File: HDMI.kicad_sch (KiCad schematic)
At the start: 38 parts, among them J1004 HDMI_D_1.4, Q1 2N7002, Q2 2SK3018, Q3 2SK3018, Q4 2SK3018, U1011 TPAZ1023-04F, U1012 TPAZ1023-04F

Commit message: commit before removing duplicated glasgow
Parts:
- renumbered C17 to C187, C1070 to C188, C1071 to C189, C1072 to C190, C1073 to C191, C1074 to C192, C1075 to C193, C1076 to C194, C1092 to C199, D1014 to D37, D1015 to D38, D1016 to D39, D1017 to D40, F1002 to F6, J1004 to J32, Q1 to Q11, Q2 to Q12, Q3 to Q13, Q4 to Q14, R1043 to R120, R1044 to R121, R1045 to R122, R1046 to R124, R1047 to R125, R1048 to R126, R1049 to R127, R1050 to R128, R1051 to R129, R1052 to R130, R1053 to R131, R1054 to R132, R1055 to R133, R1056 to R134, R1057 to R135, R1058 to R136, R1059 to R137, U1011 to U43, U1012 to U44

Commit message: went back to the drawing board
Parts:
- added C11, C14, C16, C18, C20, C22, C24, C26, C28, C30, C32, C34, C36, C38: 0.1uF, A_DFRobot:C_0402, symbol Device:C
- added C13, C15, C17, C19, C21, C23, C25, C27, C29, C31, C33, C35, C37, C39: 10nF, A_DFRobot:C_0402, symbol Device:C
- added C61, C62: 47pF, A_DFRobot:C_0402, symbol Device:C
- added C63, C64: 1uF, A_DFRobot:C_0402, symbol Device:C
- added D1, D27: RCLAMP0524PATCT, RCLAMP0524PATCT:DIO_RCLAMP0524PATCT, symbol RCLAMP0524PATCT:RCLAMP0524PATCT
- added D2: RCLAMP0524PATCT, HDMI:DIO_RCLAMP0524PATCT, symbol RCLAMP0524PATCT:RCLAMP0524PATCT
- added D28: LED, LED_SMD:LED_0603_1608Metric, symbol Device:LED
- added J3: Conn_01x03_Pin, symbol Connector:Conn_01x03_Pin
- added J4: Conn_02x01, symbol Connector_Generic:Conn_02x01
- added R10, R11, R12, R13, R14, R15, R17, R5, R6, R7, R8, R9: 0 Ohm, A_DFRobot:R_0603_1608Metric, symbol Device:R
- added R25, R26: 2k, A_DFRobot:R_0402, symbol Device:R
- added R28: 887ohm +-1%, A_DFRobot:R_0402, symbol Device:R
- added R29: 500ohm +-1%, A_DFRobot:R_0402, symbol Device:R
- added R86: 47k +-1%, A_DFRobot:R_0402, symbol Device:R
- added R87: 390k, A_DFRobot:R_0402, symbol Device:R
- added R88, R89: 51r, A_DFRobot:R_0402, symbol Device:R
- added R90: 5r1, A_DFRobot:R_0402, symbol Device:R
- added R91: 48k7, A_DFRobot:R_0402, symbol Device:R
- added R92: 220r, A_DFRobot:R_0402, symbol Device:R
- added TP2: ALSB, A_HDJ_Library:TestPoint_Pad_D1.0mm, symbol Connector:TestPoint
- added U1: ADV7623BSTZ, ST_144_ADI, symbol 2026-04-04_08-32-55:ADV7623BSTZ
- added U2: NC7SZ125M5, SC-74A-5_1P65X3P15_ONS, symbol 2026-04-05_20-11-58:NC7SZ125M5
- added Y3: ABM8G-28.63636MHZ-18-D2Y-T, CRYSTAL_ABM8G_ABR, symbol 2026-04-05_02-23-25:ABM8G-28.63636MHZ-18-D2Y-T
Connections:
- net +3V3: now also C24.1, C25.1, C26.1, C27.1, C28.1, C29.1, C30.1, C31.1, C32.1, C33.1, U1.114 (TVDD), U1.12 (TVDD), U1.120 (TVDD), U1.133 (TVDD), U1.139 (TVDD), U1.25 (TVDD), U1.31 (TVDD), U1.6 (TVDD), U1.73 (DVDDIO), U1.86 (DVDDIO), U2.5 (VCC)
- net 5V_HDMI_VCC: now also R25.1, R26.1
- net DDC_SCL: now also R14.1, U1.109 (DDCA_SCL); no longer J32.17 (SCL)
- net DDC_SDA: now also R15.1, U1.108 (DDCA_SDA); no longer J32.18 (SDA)
- net GND: now also C11.2, C13.2, C14.2, C15.2, C16.2, C17.2, C18.2, C19.2, C20.2, C21.2, C22.2, C23.2, C24.2, C25.2, C26.2, C27.2, C28.2, C29.2, C30.2, C31.2, C32.2, C33.2, C34.2, C35.2, C36.2, C37.2, C38.2, C39.2, C61.2, C62.2, D1.3_8, D2.3_8, D27.3_8, D28.1 (K), R28.2, R29.1, R90.2, R91.2, U1.104 (PGND), U1.111 (CGND), U1.117 (CGND), U1.125 (DGND), U1.130 (CGND), U1.136 (CGND), U1.17 (DGND), U1.22 (CGND), U1.28 (CGND), U1.3 (CGND), U1.35 (CGND), U1.38 (TXGND), U1.39 (TXPGND), U1.46 (TXGND), U1.49 (TXGND), U1.52 (TXGND), U1.58 (TXGND), U1.60 (DGND), U1.72 (DGNDIO), U1.80 (DGND), U1.85 (DGNDIO), U1.9 (CGND), U1.92 (DGND), U1.99 (PGND), U2.1 (*OE), U2.3 (GND), Y3.2 (GND), Y3.4 (GND)
- net HPD: now also R17.1, U1.105 (HP_CTRLA); no longer J32.1 (HPD/HEAC-)
- net TMDS_CK+: now also R11.1, U1.113 (RXA_C+); no longer J32.12 (CK+)
- net TMDS_CK-: now also R12.1, U1.112 (RXA_C-); no longer J32.14 (CK-)
- net TMDS_D0+: now also R9.1, U1.116 (RXA_0+); no longer J32.9 (D0+)
- net TMDS_D0-: now also R10.1, U1.115 (RXA_0-); no longer J32.11 (D0-)
- net TMDS_D1+: now also R7.1, U1.119 (RXA_1+); no longer J32.6 (D1+)
- net TMDS_D1-: now also R8.1, U1.118 (RXA_1-); no longer J32.8 (D1-)
- net TMDS_D2+: now also R5.1, U1.122 (RXA_2+); no longer J32.3 (D2+)
- net TMDS_D2-: now also R6.1, U1.121 (RXA_2-); no longer J32.5 (D2-)
- net CEC_STUB: now reaches J32.15 (CEC)
- net CEC_STUB: now also D27.5
- net at J32.19 (+5V): now also R13.2; no longer F6.2
- net HDMI_TX_RESERVED: now reaches J32.2 (UTILITY/HEAC+)
- net HDMI_TX_RESERVED: now also C63.2, U1.42 (ARC+)
- new net: C64.1, R89.1
- new net: R92.1, U2.4 (Y)
- new net: R28.1, U1.40 (EXT_SWING)
- new net: J3.3 (Pin_3), R86.1, TP2.1, U1.62 (ALSB)
- new net: C61.1, R87.1, U1.101 (XTAL), Y3.3
- new net: C62.1, R87.2, U1.102 (XTAL1), Y3.1
- new net: R88.2, R89.2, R90.1
- new net: D28.2 (A), R92.2
- new net: R29.2, U1.107 (RTERM)
- new net: U1.97 (*RESET), U1.98 (*PWRDN)
- new net: C63.1, R88.1
- new net +1V8: C11.1, C13.1, C14.1, C15.1, C16.1, C17.1, C18.1, C19.1, C20.1, C21.1, C22.1, C23.1, C34.1, C35.1, C36.1, C37.1, C38.1, C39.1, U1.100 (PVDD), U1.103 (PVDD), U1.110 (CVDD), U1.126 (DVDD), U1.129 (CVDD), U1.18 (DVDD), U1.2 (CVDD), U1.21 (CVDD), U1.34 (CVDD), U1.36 (TXPVDD), U1.37 (TXPLVDD), U1.45 (TXAVDD), U1.55 (TXAVDD), U1.61 (DVDD), U1.81 (DVDD), U1.93 (DVDD)
- new net 5v_hdmi_out: F6.2, R13.1, U1.106 (5V_DETA)
- new net HDMI_TX0+: D1.1, D1.10, J32.3 (D2+), R5.2, U1.51 (TX0+)
- new net HDMI_TX0-: D1.2, D1.9, J32.5 (D2-), R6.2, U1.50 (TX0-)
- new net HDMI_TX1+: D2.4, D2.7, J32.6 (D1+), R7.2, U1.54 (TX1+)
- new net HDMI_TX1-: D2.5, D2.6, J32.8 (D1-), R8.2, U1.53 (TX1-)
- new net HDMI_TX2+: D2.1, D2.10, J32.9 (D0+), R9.2, U1.57 (TX2+)
- new net HDMI_TX2-: D2.2, D2.9, J32.11 (D0-), R10.2, U1.56 (TX2-)
- new net HDMI_TXC+: D1.5, D1.6, J32.12 (CK+), R11.2, U1.48 (TXC+)
- new net HDMI_TXC-: D1.4, D1.7, J32.14 (CK-), R12.2, U1.47 (TXC-)
- new net HPD_OUT: C64.2, D27.10, J32.1 (HPD/HEAC-), R17.2, R91.1, U1.41 (HPD_ARC-), U2.2 (A)
- new net OSD_CS: U1.65 (EP_CS)
- new net OSD_MISO: U1.67 (EP_MISO)
- new net OSD_MOSI: U1.66 (EP_MOSI)
- new net OSD_SCK: U1.64 (EP_SCK)
- new net SCL: J4.2 (Pin_2), U1.79 (SCL)
- new net SDA: J4.1 (Pin_1), U1.78 (SDATA)
- new net TXDDC_SCL: D27.1, J32.18 (SDA), R15.2, R26.2, U1.44 (TXDDC_SCL)
- new net TXDDC_SDA: D27.6, J32.17 (SCL), R14.2, R25.2, U1.43 (TXDDC_SDA)
- no-connect marks 2 -> 61
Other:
- moved on the sheet: C199, F6, J32, Q12, Q13, R120, R122

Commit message: some power stuff (unfinished)
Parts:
- D1: footprint RCLAMP0524PATCT:DIO_RCLAMP0524PATCT -> HDMI:DIO_RCLAMP0524PATCT
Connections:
- net HDMI_TX0+: now also D2.1, D2.10; no longer D1.1, D1.10
- net HDMI_TX0-: now also D2.2, D2.9; no longer D1.2, D1.9
- net HDMI_TX1+: now also D1.1, D1.10; no longer D2.4, D2.7
- net HDMI_TX1-: now also D1.2, D1.9; no longer D2.5, D2.6
- net HDMI_TX2+: now also D2.4, D2.7; no longer D2.1, D2.10
- net HDMI_TX2-: now also D2.5, D2.6; no longer D2.2, D2.9
- net HDMI_TXC+: now also D1.4, D1.7; no longer D1.5, D1.6
- net HDMI_TXC-: now also D1.5, D1.6; no longer D1.4, D1.7
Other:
- moved on the sheet: D1

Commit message: hdmi-power-finished?
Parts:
- removed R13: 0 Ohm, A_DFRobot:R_0603_1608Metric, symbol Device:R
- D27: footprint RCLAMP0524PATCT:DIO_RCLAMP0524PATCT -> HDMI:DIO_RCLAMP0524PATCT
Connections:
- net 5V_HDMI_VCC: now also U1.106 (5V_DETA)
- net at J32.19 (+5V): now also F6.2
- removed net 5v_hdmi_out: F6.2, U1.106 (5V_DETA)

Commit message: V4 done ???
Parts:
- removed R14, R15, R17: 0 Ohm, A_DFRobot:R_0603_1608Metric, symbol Device:R
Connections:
- net HPD_OUT is gone; now on net HPD: C64.2, D27.10, J32.1 (HPD/HEAC-), R91.1, U1.41 (HPD_ARC-), U2.2 (A)
- net TXDDC_SCL is gone; now on net DDC_SDA: D27.1, J32.18 (SDA), R26.2, U1.44 (TXDDC_SCL)
- net TXDDC_SDA is gone; now on net DDC_SCL: D27.6, J32.17 (SCL), R25.2, U1.43 (TXDDC_SDA)
- net +3V3: now also R86.2
- net HDMI_TX0+: now also D2.2, D2.9, J32.9 (D0+), R9.2; no longer D2.1, D2.10, J32.3 (D2+), R5.2
- net HDMI_TX0-: now also D2.1, D2.10, J32.11 (D0-), R10.2; no longer D2.2, D2.9, J32.5 (D2-), R6.2
- net HDMI_TX2+: now also D2.5, D2.6, J32.3 (D2+), R5.2; no longer D2.4, D2.7, J32.9 (D0+), R9.2
- net HDMI_TX2-: now also D2.4, D2.7, J32.5 (D2-), R6.2; no longer D2.5, D2.6, J32.11 (D0-), R10.2
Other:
- moved on the sheet: R86, R88, R89, R90

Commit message: more fixes, tweaks, pretty
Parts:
- D28, R92, U2: now not fitted; now left out of the parts list
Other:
- note added: "is this ok, had to make U2 DNP"
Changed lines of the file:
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@@
 	(generator_version "10.0")
 	(paper "A2")
+	(text "is this ok, had to make U2 DNP"
+		(exclude_from_sim no)
+		(at 549.91 278.13 0)
+		(effects
+			(font
+				(size 1.27 1.27)
+			)
+		)
+	)
 	(text_box "leave floating for always on"
 		(exclude_from_sim no)
@@
 		(body_style 1)
 		(exclude_from_sim no)
-		(in_bom yes)
+		(in_bom no)
 		(on_board yes)
 		(in_pos_files yes)
-		(dnp no)
+		(dnp yes)
 		(fields_autoplaced yes)
 		(property "Reference" "#PWR023"
@@
 		(body_style 1)
 		(exclude_from_sim no)
-		(in_bom yes)
+		(in_bom no)
 		(on_board yes)
 		(in_pos_files yes)
-		(dnp no)
+		(dnp yes)
 		(fields_autoplaced yes)
 		(property "Reference" "U2"
@@
 		(body_style 1)
 		(exclude_from_sim no)
-		(in_bom yes)
+		(in_bom no)
 		(on_board yes)
 		(in_pos_files yes)
-		(dnp no)
+		(dnp yes)
 		(fields_autoplaced yes)
 		(property "Reference" "D28"
@@
 		(body_style 1)
 		(exclude_from_sim no)
-		(in_bom yes)
+		(in_bom no)
 		(on_board yes)
 		(in_pos_files yes)
-		(dnp no)
+		(dnp yes)
 		(fields_autoplaced yes)
 		(property "Reference" "#PWR020"
@@
 		(body_style 1)
 		(exclude_from_sim no)
-		(in_bom yes)
+		(in_bom no)
 		(on_board yes)
 		(in_pos_files yes)
-		(dnp no)
+		(dnp yes)
 		(fields_autoplaced yes)
 		(property "Reference" "#PWR025"
@@
 		(body_style 1)
 		(exclude_from_sim no)
-		(in_bom yes)
+		(in_bom no)
 		(on_board yes)
 		(in_pos_files yes)
-		(dnp no)
+		(dnp yes)
 		(fields_autoplaced yes)
 		(property "Reference" "#PWR030"
@@
 		(body_style 1)
 		(exclude_from_sim no)
-		(in_bom yes)
+		(in_bom no)
 		(on_board yes)
 		(in_pos_files yes)
-		(dnp no)
+		(dnp yes)
 		(fields_autoplaced yes)
 		(property "Reference" "R92"

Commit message: last push before editing with the grid view (gonna break everything)
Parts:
- C11, C14, C16, C18, C20, C22, C24: value 0.1uF -> u1; MPN (none) -> TMK105BJ104KV-F
- C13, C15, C17, C19, C21, C23, C25: value 10nF -> 10n; MPN (none) -> C0402C103K5RACTU
- C187, C188, C189, C190, C191, C192, C193, C194: value 100nF/16V -> 100n; DF_Comment 贴片电容0402-100nF-16V-X7R(0402) -> (none); MPN (none) -> 478-KGM05CR71H104KHCT-ND
- C199: value 100nF/16V -> 100n; MPN (none) -> 478-KGM05CR71H104KHCT-ND
- C26, C28, C30, C32, C34, C36, C38: value 0.1uF -> 10n; MPN (none) -> C0402C103K5RACTU
- C27, C29, C31, C33, C35, C37, C39: value 10nF -> u1; MPN (none) -> TMK105BJ104KV-F
- C61, C62: value 47pF -> 47p; MPN (none) -> C0402C470J5GACTU
- C63, C64: value 1uF -> 1u; MPN (none) -> 0402ZG105ZAT2A
- D1, D2, D27: MP RCLAMP0524PATCT -> (none); MPN (none) -> RCLAMP0524PATCT
- D37, D38: MPN (none) -> 0402ESDA-05N
- D39: MPN (none) -> https://www.onsemi.com/pub/Collateral/ESD9B-D.PDF
- D40: MPN (none) -> 1N5819WS
- Q11: MPN (none) -> 2N7002
- Q12, Q13, Q14: MPN (none) -> 2SK3018
- R120, R133, R136: value 2.2K/1% -> 2K2; MPN (none) -> RC0402FR-132K2L
- R121: value 1M/1% -> 1M; DF_Comment 贴片电阻0402-1M-1% -> (none); MPN (none) -> 560112110033
- R122, R137: value 2.2K/1% -> 2K2; DF_Comment 贴片电阻0402-2.2K-1% -> (none); MPN (none) -> RC0402FR-132K2L
- R124: value 21.5K/1% -> 21K5; DF_Comment 贴片电阻0402-21.5K-1% -> (none); MPN (none) -> RCG040221K5FKED
- R125, R126, R127, R128, R131, R132, R134, R135: value 470R/1% -> 470; MPN (none) -> C2889341
- R129: value 1K/1% -> 1K; DF_Comment 贴片电阻0402-1K-1% -> (none); MPN (none) -> RMCF0402FT1K00
- R28: value 887ohm +-1% -> 887; MPN (none) -> RC0402JR-070RL
- R29: value 500ohm +-1% -> 500; MPN (none) -> PNM0402E5000BST1
- R86: value 47k +-1% -> 47K; MPN (none) -> ERA-2AEB473X
- R87: value 390k -> 390K; MPN (none) -> ESR01MZPF3903
- R88, R89: value 51r -> 51; MPN (none) -> ERJ-2RKF51R0X
- R90: MPN (none) -> ERJ-2RKF5101X
- R91: value 48k7 -> 48K7; MPN (none) -> TNPW040248K7BEED
- U1: MPN (none) -> ADV7623BSTZ
- U43, U44: MPN (none) -> TPAZ1023-04F
- Y3: MPN (none) -> ABM8G-28.63636MHZ-18-D2Y-T

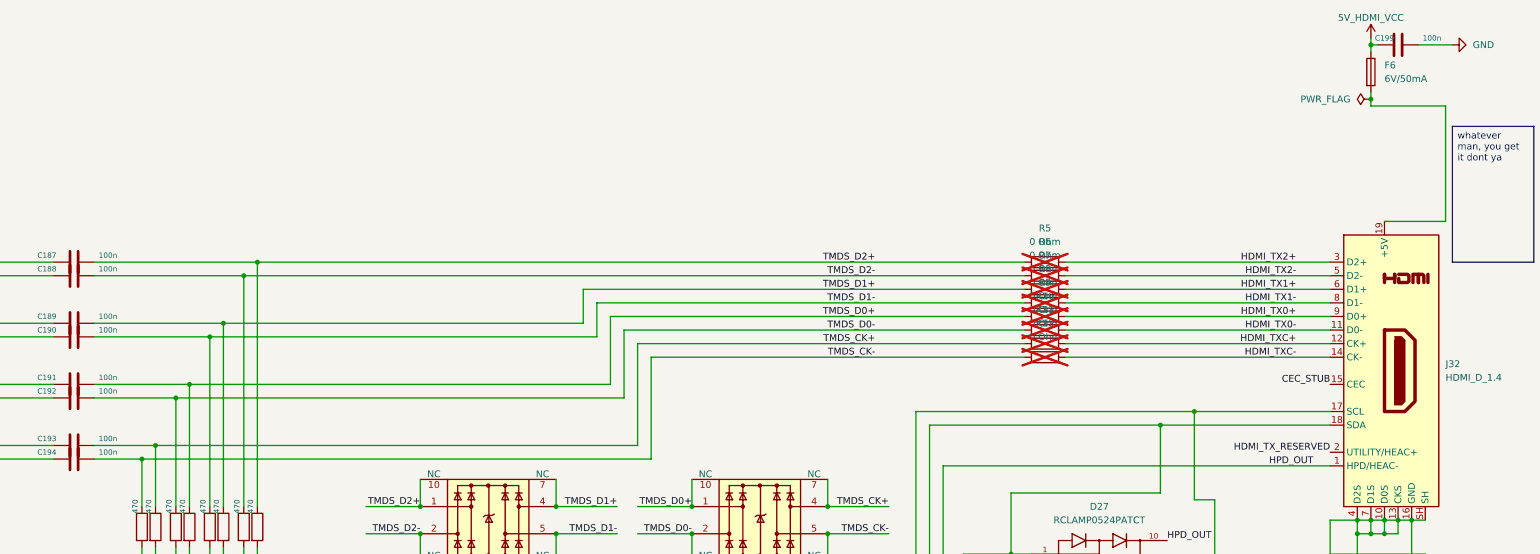
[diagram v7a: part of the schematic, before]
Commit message: added MPN to all parts by hand :'(
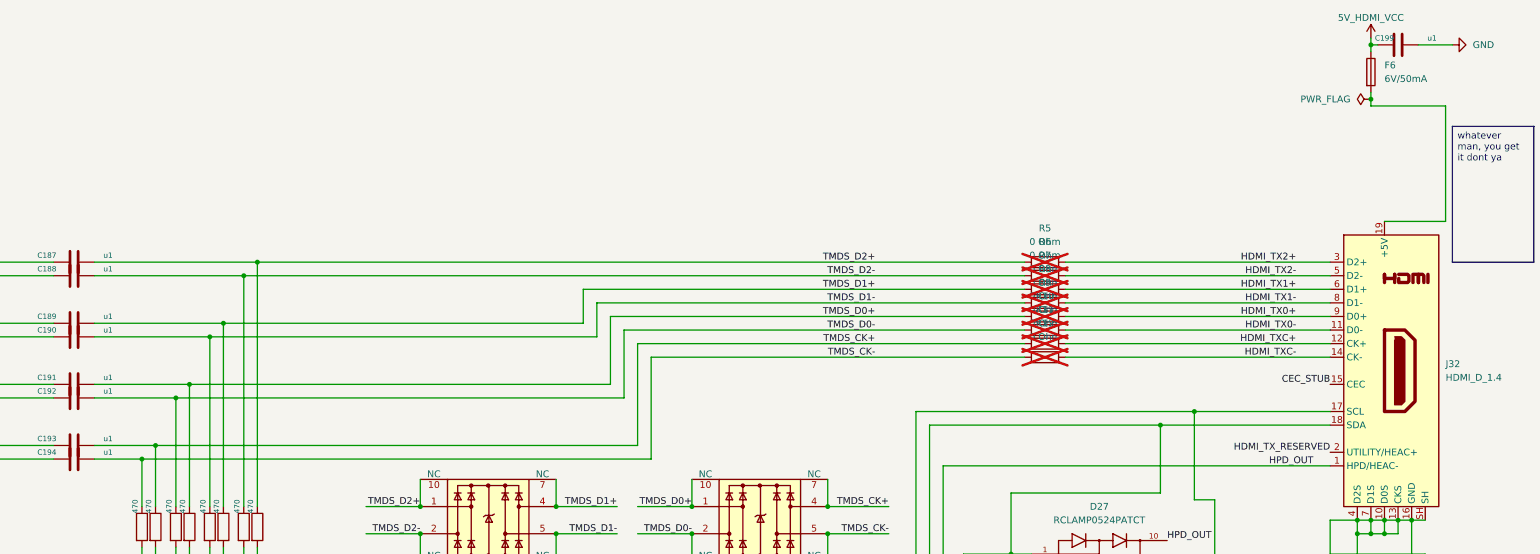
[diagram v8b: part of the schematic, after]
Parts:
- C11, C14, C16, C18, C20, C22, C24, C27, C29, C31, C33, C35, C37, C39: MPN TMK105BJ104KV-F -> C1005X7R1H104K050BE
- C187, C188, C189, C190, C191, C192, C193, C194, C199: value 100n -> u1; MPN 478-KGM05CR71H104KHCT-ND -> C1005X7R1H104K050BE
- D39: MPN https://www.onsemi.com/pub/Collateral/ESD9B-D.PDF -> 0402ESDA-05N
- F6: MPN (none) -> C7472508
- J32: MPN (none) -> 0467651001
- R120, R122, R133, R136, R137: MPN RC0402FR-132K2L -> RCS04022K20FKED
- R125, R126, R127, R128, R131, R132, R134, R135: DF_Comment 贴片电阻0402-470R-1% -> (none); MPN C2889341 -> ERJ-2RKF4700X
- R129: MPN RMCF0402FT1K00 -> RCS04021K00JNED
- R25, R26: MPN (none) -> RCS04022K00FKED
- TP2: now left out of the parts list
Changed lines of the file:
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@@
 			)
 		)
-		(property "MPN" "TMK105BJ104KV-F"
+		(property "MPN" "C1005X7R1H104K050BE"
 			(at 410.21 76.2 0)
 			(hide yes)
@@
 			)
 		)
-		(property "MPN" "TMK105BJ104KV-F"
+		(property "MPN" "C1005X7R1H104K050BE"
 			(at 439.42 86.36 0)
 			(hide yes)
@@
 			)
 		)
-		(property "MPN" "TMK105BJ104KV-F"
+		(property "MPN" "C1005X7R1H104K050BE"
 			(at 430.53 50.8 0)
 			(hide yes)
@@
 			)
 		)
-		(property "DF_Comment" "贴片电阻0402-470R-1%"
+		(property "DF_Comment" ""
 			(at 143.51 110.49 0)
 			(hide yes)
@@
 			)
 		)
-		(property "MPN" "C2889341"
+		(property "MPN" "ERJ-2RKF4700X"
 			(at 143.51 110.49 0)
 			(hide yes)
@@
 			)
 		)
-		(property "Value" "100n"
+		(property "Value" "u1"
 			(at 363.22 19.05 90)
 			(show_name no)
@@
 			)
 		)
-		(property "MPN" "478-KGM05CR71H104KHCT-ND"
+		(property "MPN" "C1005X7R1H104K050BE"
 			(at 356.87 20.32 0)
 			(hide yes)
@@
 			)
 		)
-		(property "MPN" "TMK105BJ104KV-F"
+		(property "MPN" "C1005X7R1H104K050BE"
 			(at 469.9 114.3 0)
 			(hide yes)
@@
 			)
 		)
-		(property "MPN" "RC0402FR-132K2L"
+		(property "MPN" "RCS04022K20FKED"
 			(at 157.48 133.35 0)
 			(hide yes)
@@
 			)
 		)
-		(property "Value" "100n"
+		(property "Value" "u1"
 			(at 115.57 93.98 90)
 			(show_name no)
@@
 			)
 		)
-		(property "MPN" "478-KGM05CR71H104KHCT-ND"
+		(property "MPN" "C1005X7R1H104K050BE"
 			(at 109.22 95.25 0)
 			(hide yes)
@@
 			)
 		)
-		(property "Value" "100n"
+		(property "Value" "u1"
 			(at 115.57 73.66 90)
 			(show_name no)
@@
 			)
 		)
-		(property "MPN" "478-KGM05CR71H104KHCT-ND"
+		(property "MPN" "C1005X7R1H104K050BE"
 			(at 109.22 74.93 0)
 			(hide yes)
@@
 			)
 		)
-		(property "DF_Comment" "贴片电阻0402-470R-1%"
+		(property "DF_Comment" ""
 			(at 140.97 110.49 0)
 			(hide yes)
@@
 			)
 		)
-		(property "MPN" "C2889341"
+		(property "MPN" "ERJ-2RKF4700X"
 			(at 140.97 110.49 0)
 			(hide yes)
@@
 			)
 		)
+		(property "MPN" "RCS04022K00FKED"
+			(at 326.39 156.21 0)
+			(hide yes)
+			(show_name no)
+			(do_not_autoplace no)
+			(effects
+				(font
+					(size 1.27 1.27)
+				)
+			)
+		)
 		(pin "1"
 		)
@@
 			)
 		)
-		(property "MPN" "TMK105BJ104KV-F"
+		(property "MPN" "C1005X7R1H104K050BE"
 			(at 444.5 46.99 0)
 			(hide yes)
@@
 			)
 		)
-		(property "MPN" "TMK105BJ104KV-F"
+		(property "MPN" "C1005X7R1H104K050BE"
 			(at 424.18 80.01 0)
 			(hide yes)
@@
 			)
 		)
-		(property "MPN" "TMK105BJ104KV-F"
+		(property "MPN" "C1005X7R1H104K050BE"
 			(at 457.2 39.37 0)
 			(hide yes)
@@
 			)
 		)
-		(property "MPN" "RC0402FR-132K2L"
+		(property "MPN" "RCS04022K20FKED"
 			(at 85.09 153.67 0)
 			(hide yes)
@@
 			)
 		)
-		(property "DF_Comment" "贴片电阻0402-470R-1%"
+		(property "DF_Comment" ""
 			(at 124.46 110.49 0)
 			(hide yes)
@@
 			)
 		)
-		(property "MPN" "C2889341"
+		(property "MPN" "ERJ-2RKF4700X"
 			(at 124.46 110.49 0)
 			(hide yes)
@@
 			)
 		)
-		(property "MPN" "TMK105BJ104KV-F"
+		(property "MPN" "C1005X7R1H104K050BE"
 			(at 485.14 106.68 0)
 			(hide yes)
@@
 			)
 		)
-		(property "DF_Comment" "贴片电阻0402-470R-1%"
+		(property "DF_Comment" ""
 			(at 121.92 110.49 0)
 			(hide yes)
@@
 			)
 		)
-		(property "MPN" "C2889341"
+		(property "MPN" "ERJ-2RKF4700X"
 			(at 121.92 110.49 0)
 			(hide yes)
@@
 		(body_style 1)
 		(exclude_from_sim no)
-		(in_bom yes)
+		(in_bom no)
 		(on_board yes)
 		(in_pos_files yes)
@@
 			)
 		)
-		(property "MPN" "TMK105BJ104KV-F"
+		(property "MPN" "C1005X7R1H104K050BE"
 			(at 454.66 91.44 0)
 			(hide yes)
@@
 			)
 		)
-		(property "MPN" "https://www.onsemi.com/pub/Collateral/ESD9B-D.PDF"
+		(property "MPN" "0402ESDA-05N"
 			(at 148.59 193.04 0)
 			(hide yes)
@@
 			)
 		)
-		(property "Value" "100n"
+		(property "Value" "u1"
 			(at 115.57 96.52 90)
 			(show_name no)
@@
 			)
 		)
-		(property "MPN" "478-KGM05CR71H104KHCT-ND"
+		(property "MPN" "C1005X7R1H104K050BE"
 			(at 109.22 97.79 0)
 			(hide yes)
@@
 			)
 		)
-		(property "DF_Comment" "贴片电阻0402-470R-1%"
+		(property "DF_Comment" ""
 			(at 130.81 110.49 0)
 			(hide yes)
@@
 			)
 		)
-		(property "MPN" "C2889341"
+		(property "MPN" "ERJ-2RKF4700X"
 			(at 130.81 110.49 0)
 			(hide yes)
@@
 			)
 		)
-		(property "Value" "100n"
+		(property "Value" "u1"
 			(at 115.57 82.55 90)
 			(show_name no)
@@
 			)
 		)
-		(property "MPN" "478-KGM05CR71H104KHCT-ND"
+		(property "MPN" "C1005X7R1H104K050BE"
 			(at 109.22 83.82 0)
 			(hide yes)
@@
 			)
 		)
-		(property "DF_Comment" "贴片电阻0402-470R-1%"
+		(property "DF_Comment" ""
 			(at 134.62 110.49 0)
 			(hide yes)
@@
 			)
 		)
-		(property "MPN" "C2889341"
+		(property "MPN" "ERJ-2RKF4700X"
 			(at 134.62 110.49 0)
 			(hide yes)
@@
 			)
 		)
-		(property "MPN" "RC0402FR-132K2L"
+		(property "MPN" "RCS04022K20FKED"
 			(at 138.43 153.67 0)
 			(hide yes)
@@
 			)
 		)
-		(property "Value" "100n"
+		(property "Value" "u1"
 			(at 115.57 59.69 90)
 			(show_name no)
@@
 			)
 		)
-		(property "MPN" "478-KGM05CR71H104KHCT-ND"
+		(property "MPN" "C1005X7R1H104K050BE"
 			(at 109.22 60.96 0)
 			(hide yes)
@@
 			)
 		)
-		(property "DF_Comment" "贴片电阻0402-470R-1%"
+		(property "DF_Comment" ""
 			(at 137.16 110.49 0)
 			(hide yes)
@@
 			)
 		)
-		(property "MPN" "C2889341"
+		(property "MPN" "ERJ-2RKF4700X"
 			(at 137.16 110.49 0)
 			(hide yes)
@@
 			)
 		)
-		(property "MPN" "RC0402FR-132K2L"
+		(property "MPN" "RCS04022K20FKED"
 			(at 74.93 153.67 0)
 			(hide yes)
@@
 			)
 		)
-		(property "Value" "100n"
+		(property "Value" "u1"
 			(at 115.57 71.12 90)
 			(show_name no)
@@
 			)
 		)
-		(property "MPN" "478-KGM05CR71H104KHCT-ND"
+		(property "MPN" "C1005X7R1H104K050BE"
 			(at 109.22 72.39 0)
 			(hide yes)
@@
 			)
 		)
-		(property "MPN" "RMCF0402FT1K00"
+		(property "MPN" "RCS04021K00JNED"
 			(at 130.81 215.9 0)
 			(hide yes)
@@
 			)
 		)
+		(property "MPN" "RCS04022K00FKED"
+			(at 318.77 156.21 0)
+			(hide yes)
+			(show_name no)
+			(do_not_autoplace no)
+			(effects
+				(font
+					(size 1.27 1.27)
+				)
+			)
+		)
 		(pin "1"
 		)
@@
 			)
 		)
-		(property "MPN" "TMK105BJ104KV-F"
+		(property "MPN" "C1005X7R1H104K050BE"
 			(at 468.63 99.06 0)
 			(hide yes)
@@
 			)
 		)
-		(property "MPN" "TMK105BJ104KV-F"
+		(property "MPN" "C1005X7R1H104K050BE"
 			(at 416.56 55.88 0)
 			(hide yes)
@@
 			)
 		)
-		(property "DF_Comment" "贴片电阻0402-470R-1%"
+		(property "DF_Comment" ""
 			(at 128.27 110.49 0)
 			(hide yes)
@@
 			)
 		)
-		(property "MPN" "C2889341"
+		(property "MPN" "ERJ-2RKF4700X"
 			(at 128.27 110.49 0)
 			(hide yes)
@@
 			)
 		)
-		(property "MPN" "TMK105BJ104KV-F"
+		(property "MPN" "C1005X7R1H104K050BE"
 			(at 472.44 35.56 0)
 			(hide yes)
@@
 			)
 		)
+		(property "MPN" "  0467651001"
+			(at 354.33 81.28 0)
+			(hide yes)
+			(show_name no)
+			(do_not_autoplace no)
+			(effects
+				(font
+					(size 1.27 1.27)
+				)
+			)
+		)
 		(pin "SH"
 		)
@@
 			)
 		)
-		(property "MPN" "TMK105BJ104KV-F"
-			(at 400.05 63.5 0)
-			(hide yes)
-			(show_name no)
-			(do_not_autoplace no)
-			(effects
-				(font
-					(size 1.27 1.27)
-				)
-			)
-		)
-		(property "Field6" ""
+		(property "MPN" "C1005X7R1H104K050BE"
 			(at 400.05 63.5 0)
 			(hide yes)
@@
 			)
 		)
-		(property "Value" "100n"
+		(property "Value" "u1"
 			(at 115.57 85.09 90)
 			(show_name no)
@@
 			)
 		)
-		(property "MPN" "478-KGM05CR71H104KHCT-ND"
+		(property "MPN" "C1005X7R1H104K050BE"
 			(at 109.22 86.36 0)
 			(hide yes)
@@
 			)
 		)
-		(property "MPN" "TMK105BJ104KV-F"
+		(property "MPN" "C1005X7R1H104K050BE"
 			(at 483.87 30.48 0)
 			(hide yes)
@@
 			)
 		)
-		(property "Value" "100n"
+		(property "Value" "u1"
 			(at 115.57 62.23 90)
 			(show_name no)
@@
 			)
 		)
-		(property "MPN" "478-KGM05CR71H104KHCT-ND"
+		(property "MPN" "C1005X7R1H104K050BE"
 			(at 109.22 63.5 0)
 			(hide yes)
@@
 			)
 		)
-		(property "MPN" "RC0402FR-132K2L"
+		(property "MPN" "RCS04022K20FKED"
 			(at 148.59 153.67 0)
 			(hide yes)
@@
 			)
 		)
-		(property "Field-1" ""
+		(property "MPN" "C7472508"
 			(at 351.79 25.4 0)
 			(hide yes)
